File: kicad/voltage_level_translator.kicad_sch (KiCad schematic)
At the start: 16 parts, among them Q1 2N7002, SW1 TA-3532S-A2, U3 TMUX1574PW, U7 TMUX1574PW, U8 TXS0108EPW, U9 TXS0108EPW

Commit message: Modified voltage switching circuit
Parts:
- removed Q1: 2N7002, Package_TO_SOT_SMD:SOT-23, symbol Transistor_FET:2N7002
- removed R1: 10k, Resistor_SMD:R_0805_2012Metric, symbol Device:R
- R2: value 1k -> 10k
- R5: renamed from R6; value 10k -> 1k
- renumbered C6 to C1, C5 to C2, R4 to R3, R3 to R4, U8 to U1, U9 to U2, U7 to U4
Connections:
- net GATE is gone; now on net SEL: R5.1, U2.10 (OE)
- net +3.3V: now also D1.2 (A), D2.2 (A), D3.2 (A), R2.2; no longer SW1.7
- net D1_K: no longer R2.2
- net GND: now also SW1.7; no longer R2.1, R3.2, R4.2
- net SEL: now also R2.1, SW1.8
- net D1_A renamed 5V_SEL
- net 5V_SEL: now also R3.2; no longer D1.2 (A)
- net D2_A renamed 3V3_SEL
- net 3V3_SEL: now also R4.2; no longer D2.2 (A)
- removed net D3_A: D3.2 (A), SW1.8
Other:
- moved on the sheet: D1, D2, D3, R2, R3, R4, R5, SW1

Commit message: Added the inverter N-MOS
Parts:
- added Q2: 2N7002, Package_TO_SOT_SMD:SOT-23, symbol Transistor_FET:2N7002
- added R1: 10k, Resistor_SMD:R_0805_2012Metric, symbol Device:R
- renumbered C2 to C5, C1 to C6, R4 to R3, R3 to R4, R5 to R6, R2 to R?, U4 to U7, U1 to U8, U2 to U9
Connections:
- net +3.3V: now also R1.2
- net GND: now also Q2.2 (S)
- net SEL: now also Q2.1 (G); no longer U9.10 (OE)
- new net ~{SEL}: Q2.3 (D), R1.1, U9.10 (OE)
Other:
- note added: "OE = ~{SEL}"
- note removed: "GATE = OE = !SEL"

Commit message: Minor pcb modifications
- Modified capacitors for multiplexers to 4.7u
- Added bypass capacitors near  TXS0108EPW VCCA and VCCB
- Changed some text on the main schematic
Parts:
- added C1, C2, C8, C9: 0.1u, Capacitor_SMD:C_0805_2012Metric, symbol Device:C
- C5, C6: value 0.1u -> 4.7u
- gave numbers to parts that had none: 1
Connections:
- net +1V8: now also C2.1
- net +3.3V: now also C1.1, C9.1
- net GND: now also C1.2, C2.2, C8.2, C9.2
- net VTARGET: now also C8.1
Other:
- note added: "LEDs and inverter N-MOS"
- note removed: "LEDs"
- moved on the sheet: D1, D2, D3, Q2, R1, R2, R3, R4, R6, SW1

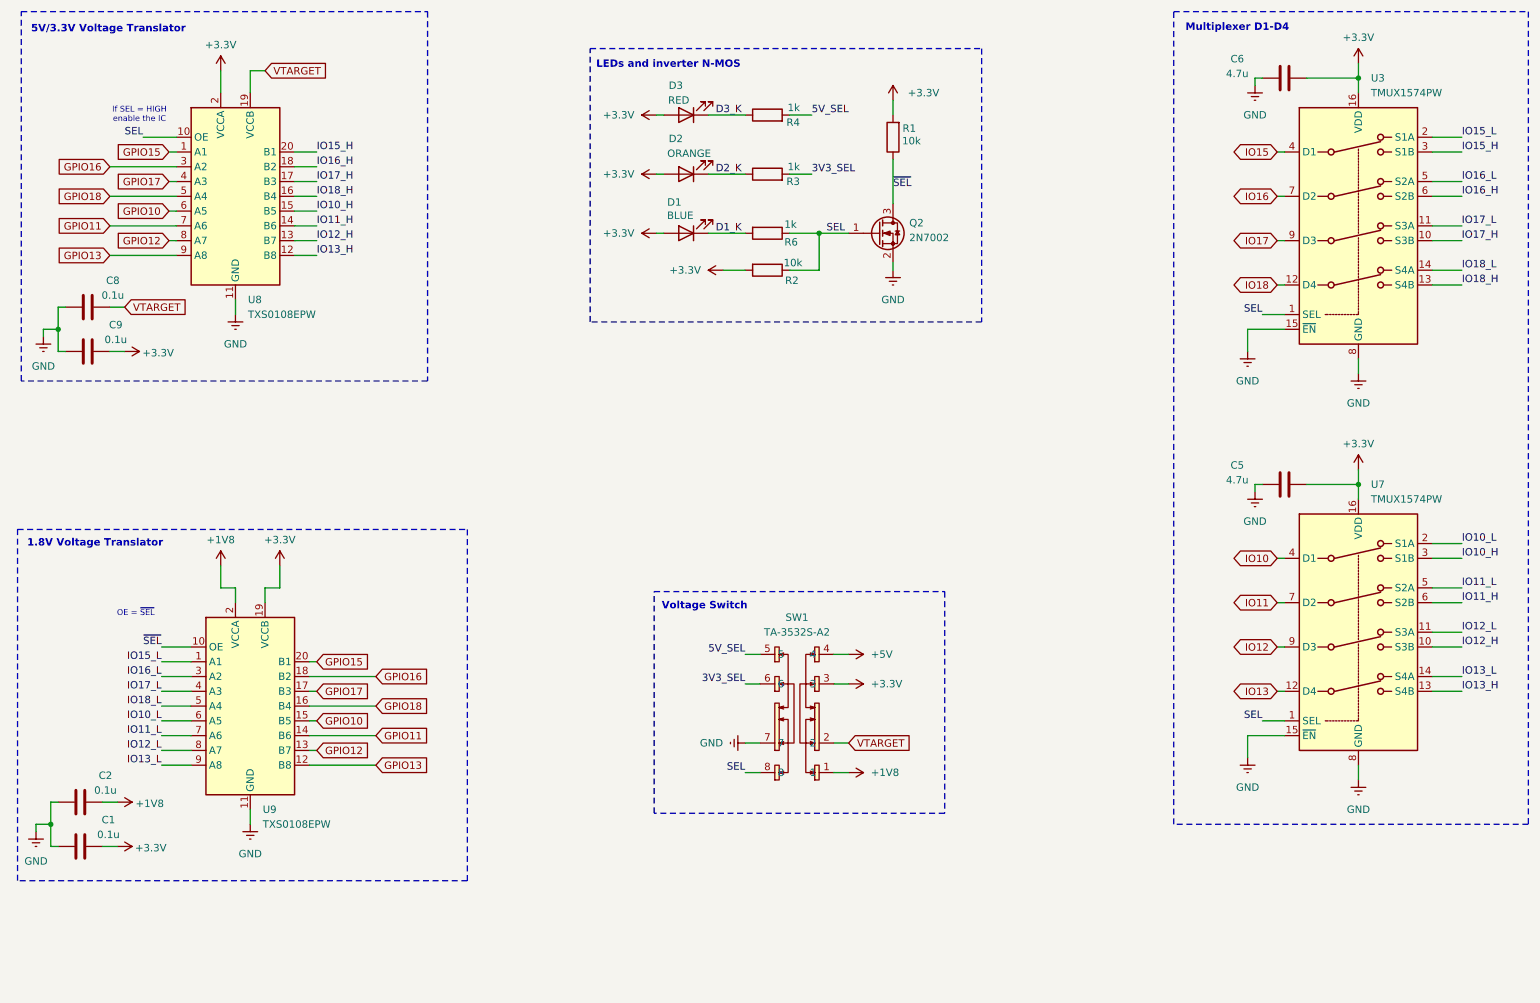
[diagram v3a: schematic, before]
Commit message: Added Analog Switch
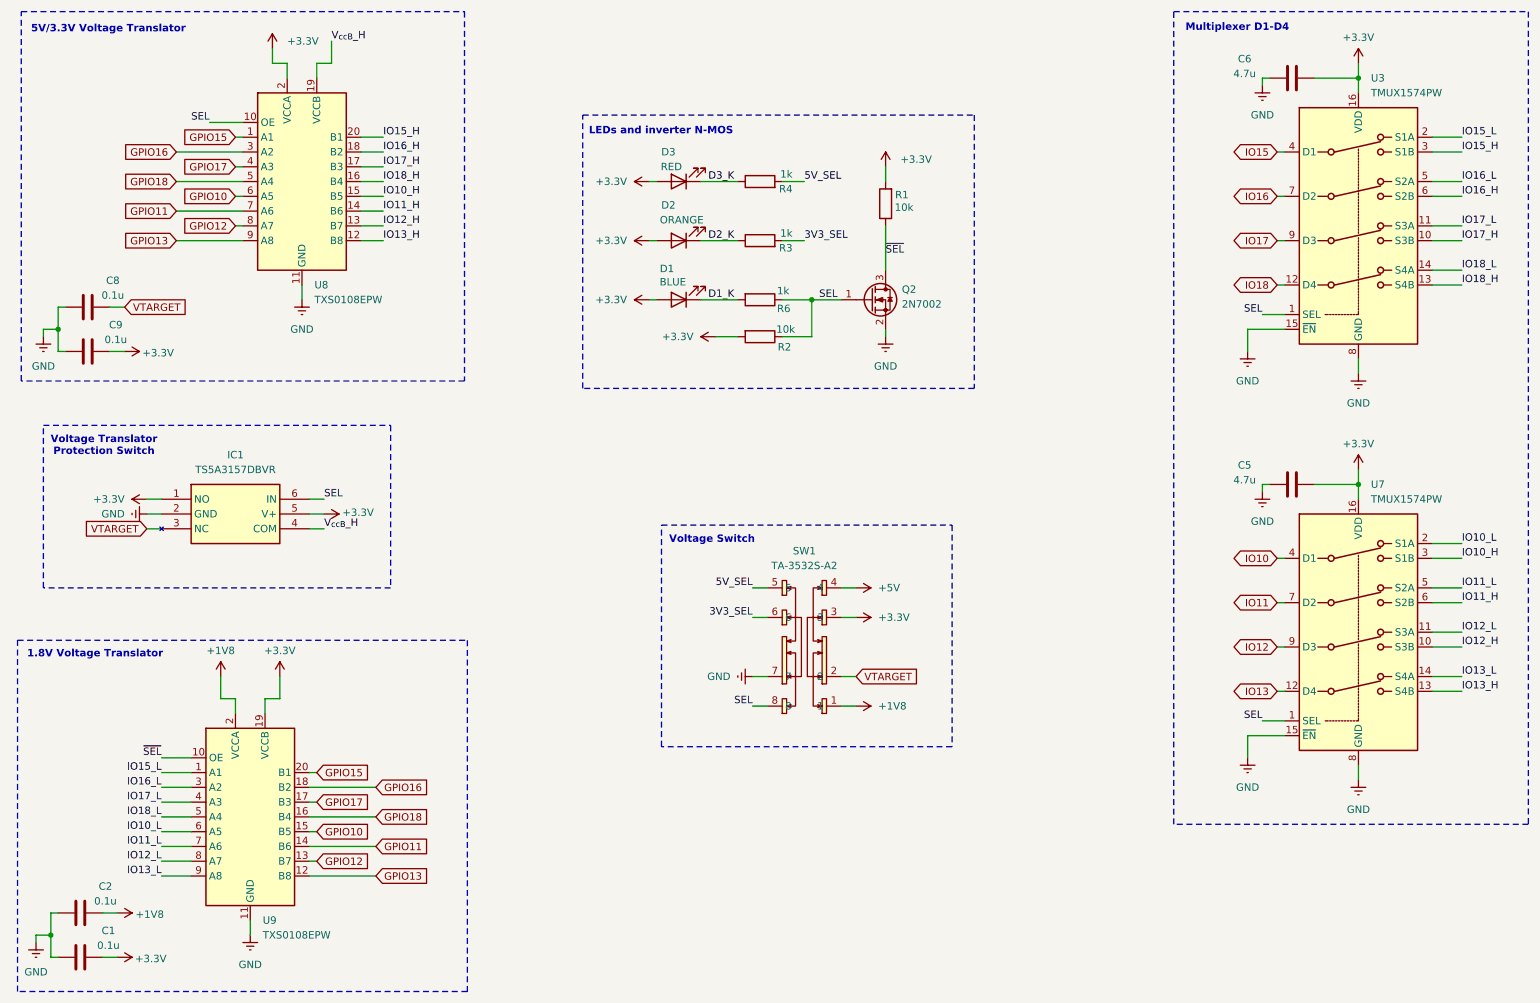
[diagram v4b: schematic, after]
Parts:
- added IC1: TS5A3157DBVR, SOT95P280X145-6N, symbol TS5A3157DBVR:TS5A3157DBVR
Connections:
- net +3.3V: now also IC1.1 (NO), IC1.5 (V+)
- net GND: now also IC1.2 (GND)
- net SEL: now also IC1.6 (IN)
- net VTARGET: now also IC1.3 (NC); no longer U8.19 (VCCB)
- new net V_{ccB}_H: IC1.4 (COM), U8.19 (VCCB)
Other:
- note added: "Voltage Translator Protection Switch"
- note removed: "If SEL = HIGH enable the IC"
- note removed: "OE = ~{SEL}"
- moved on the sheet: C1, C2, C5, C6, D1, D2, D3, Q2, R1, R2, R3, R4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

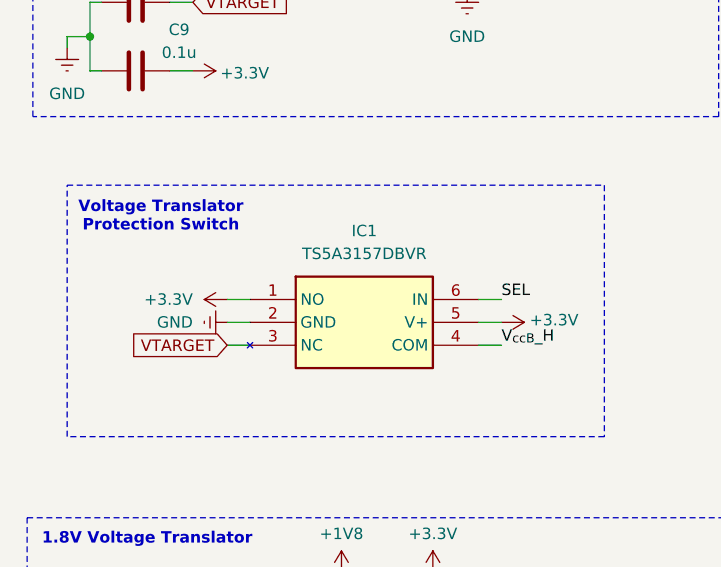
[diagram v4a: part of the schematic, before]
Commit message: New components PCB placement
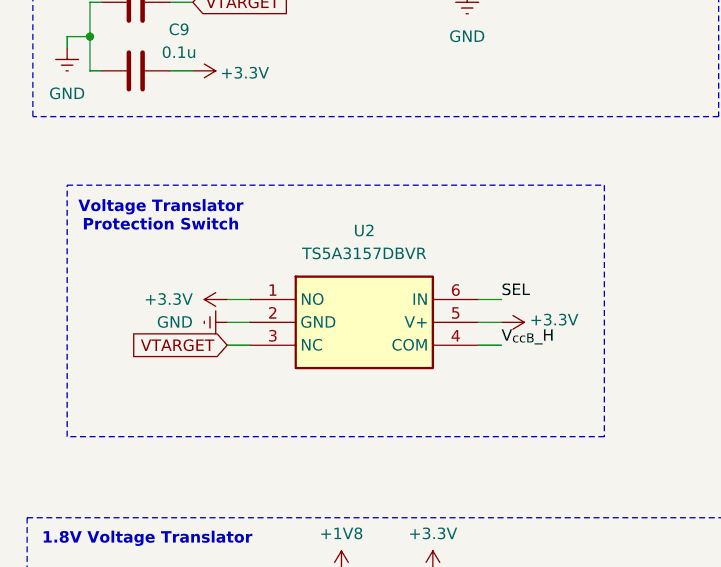
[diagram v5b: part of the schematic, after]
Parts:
- U2: renamed from IC1; footprint SOT95P280X145-6N -> TS5A3157:SOT95P280X145-6N
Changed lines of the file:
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@@
 		(dnp no)
 		(fields_autoplaced yes)
-		(property "Reference" "IC1"
+		(property "Reference" "U2"
 			(at 55.88 95.25 0)
 			(effects
@@
 			)
 		)
-		(property "Footprint" "SOT95P280X145-6N"
+		(property "Footprint" "TS5A3157:SOT95P280X145-6N"
 			(at 64.77 197.79 0)
 			(effects
@@
 			(project ""
 				(path "/07b4bde2-66d8-4845-8f7d-da280a4d29f6/4e83f8d5-a547-42b8-8426-b71a9f8b331b"
-					(reference "IC1")
+					(reference "U2")
 					(unit 1)
 				)

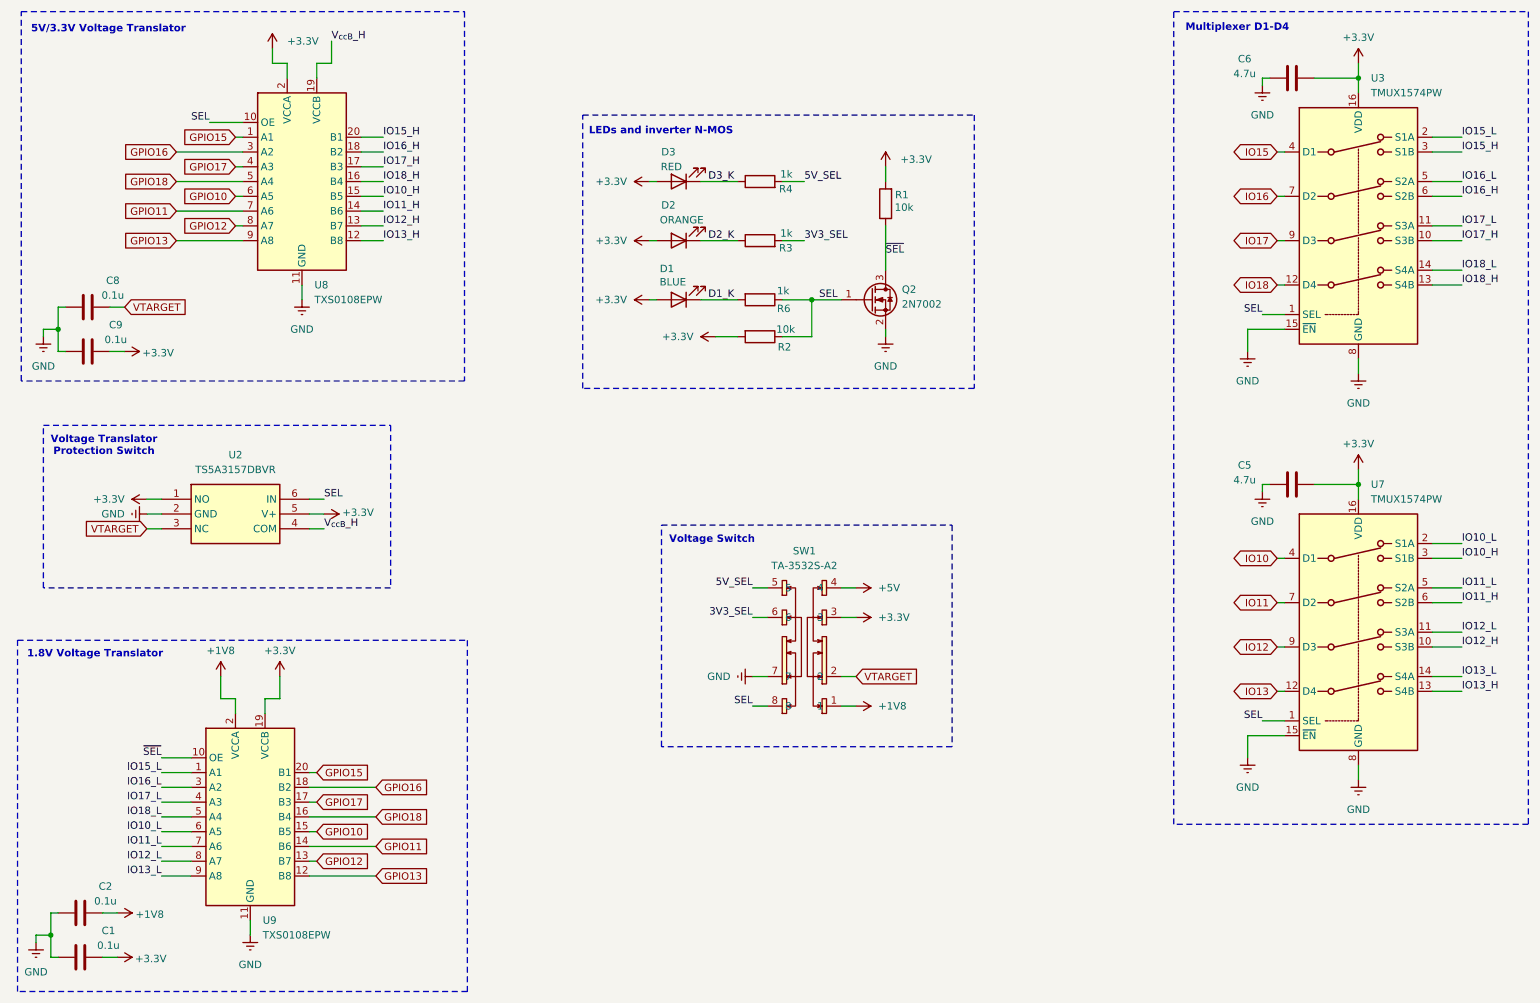
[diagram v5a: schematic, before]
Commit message: Negated switch OE
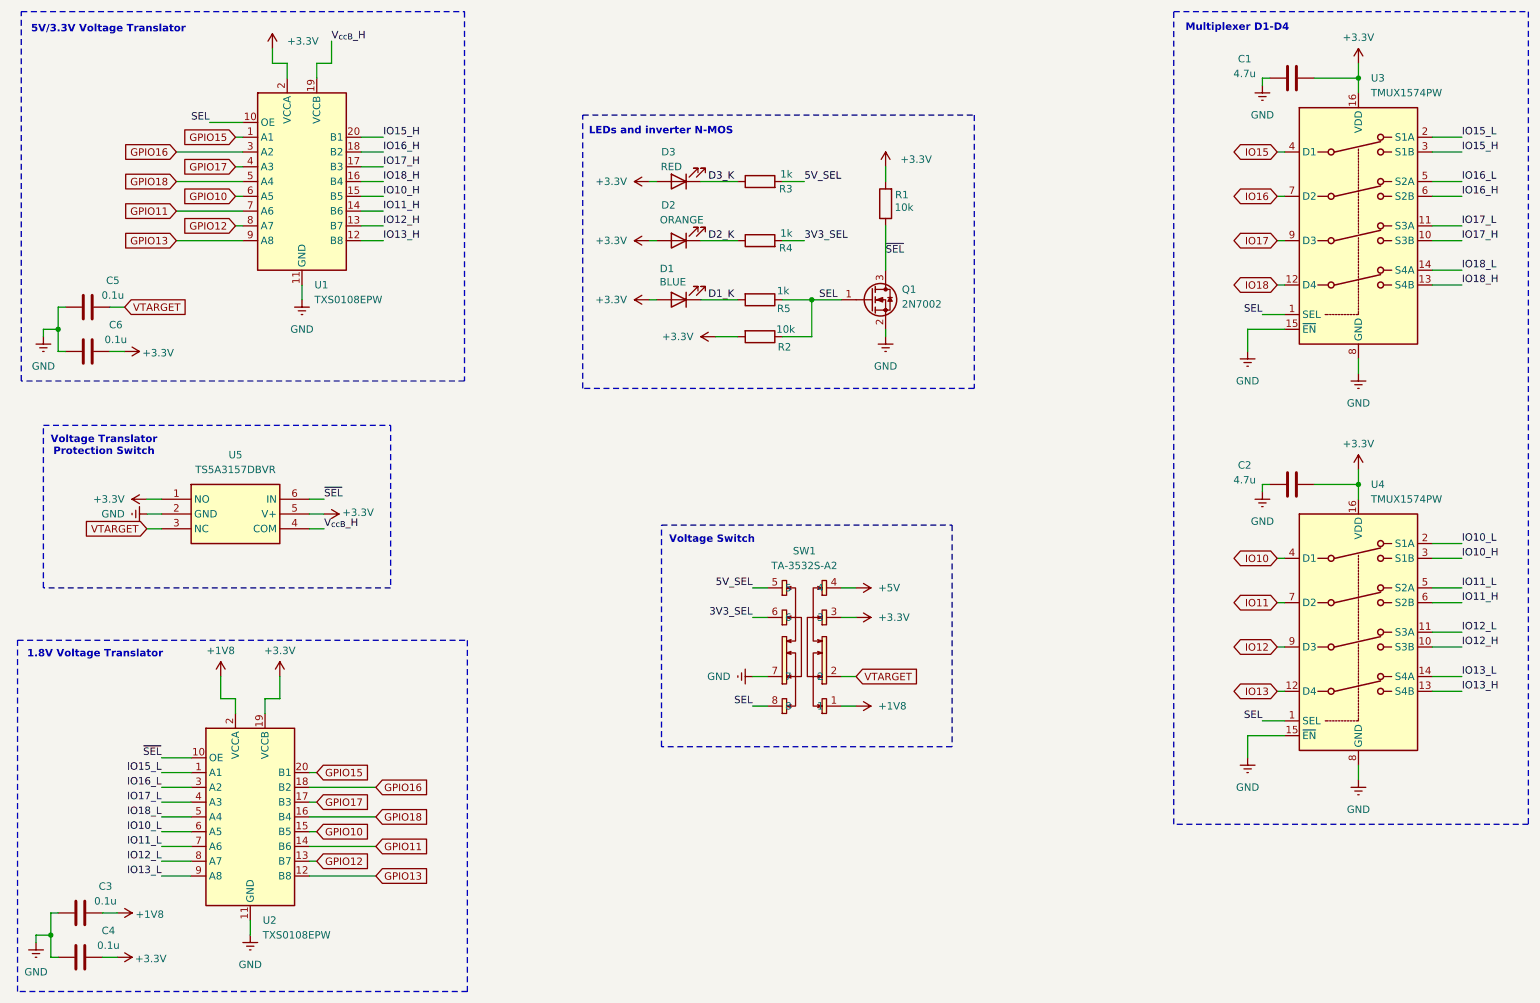
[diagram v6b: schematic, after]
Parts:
- renumbered C6 to C1, C5 to C2, C2 to C3, C1 to C4, C8 to C5, C9 to C6, Q2 to Q1, R4 to R3, R3 to R4, R6 to R5, U8 to U1, U9 to U2, U7 to U4, U2 to U5
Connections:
- net SEL: no longer U5.6 (IN)
- net ~{SEL}: now also U5.6 (IN)

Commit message: Updated PCB placement
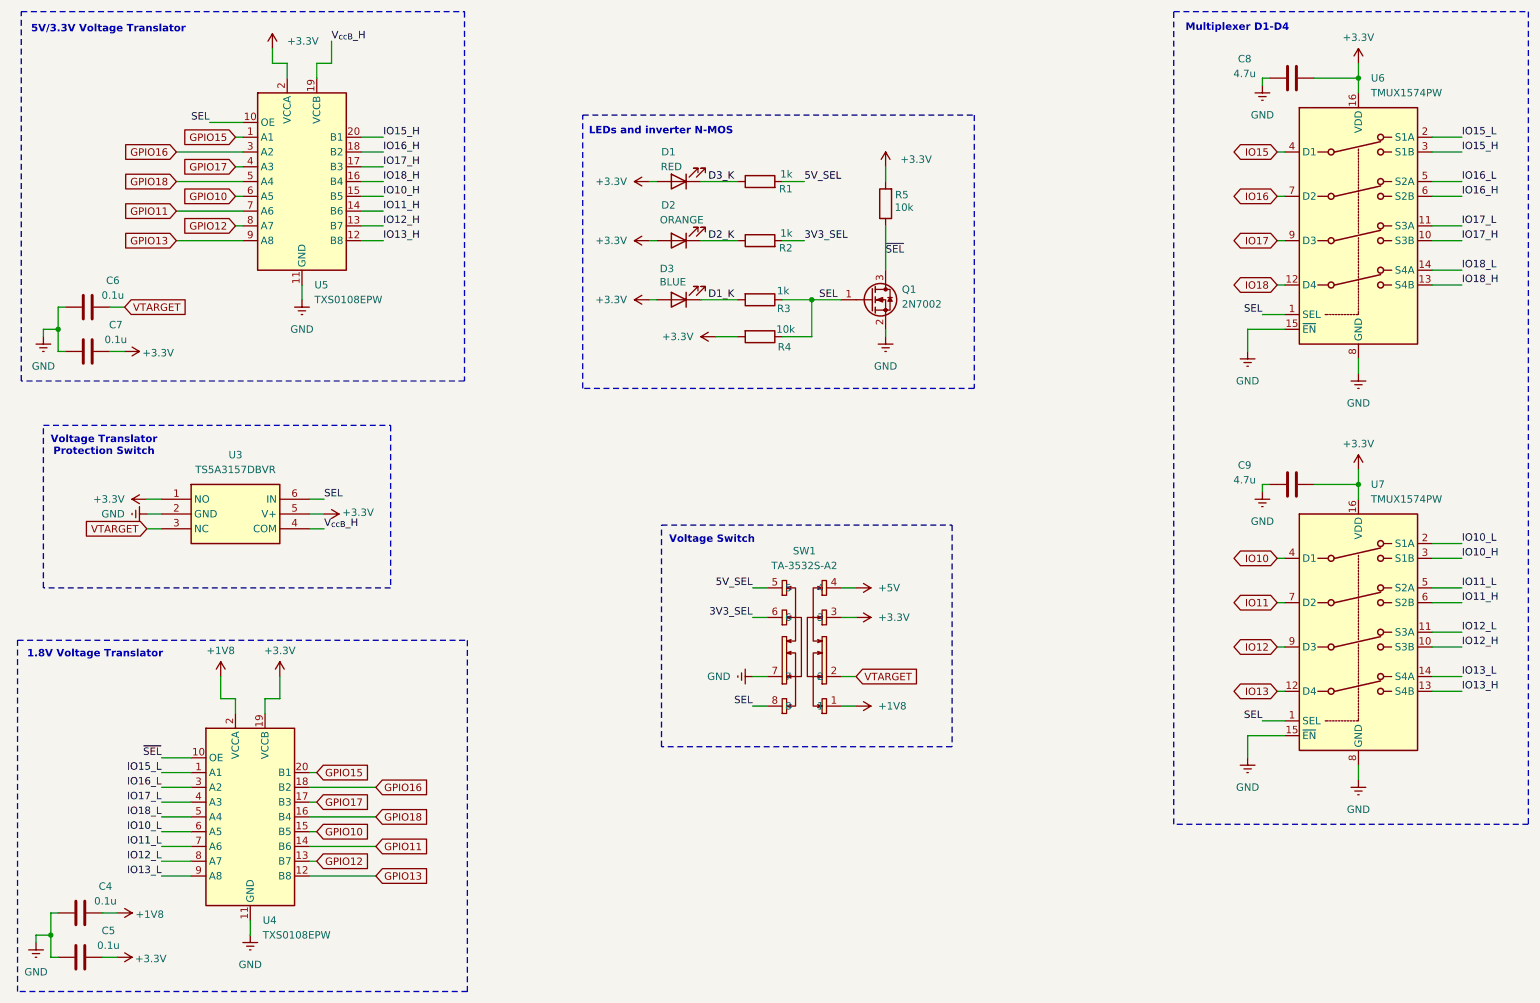
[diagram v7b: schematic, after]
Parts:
- renumbered C3 to C4, C4 to C5, C5 to C6, C6 to C7, C1 to C8, C2 to C9, D3 to D1, D1 to D3, R3 to R1, R4 to R2, R5 to R3, R2 to R4, R1 to R5, U5 to U3, U2 to U4, U1 to U5, U3 to U6, U4 to U7
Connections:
- net SEL: now also U3.6 (IN)
- net ~{SEL}: no longer U3.6 (IN)
